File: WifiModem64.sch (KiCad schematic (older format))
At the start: 29 parts, among them J1 C64-UserPort, J2 USB_B, Q1 BSS138, Q2 BSS138, Q3 BSS138, Q4 BSS138, SW1 Push, SW2 Reset, U1 WeMos_mini, U2 WeMos_D1_mini_OLED_Shield

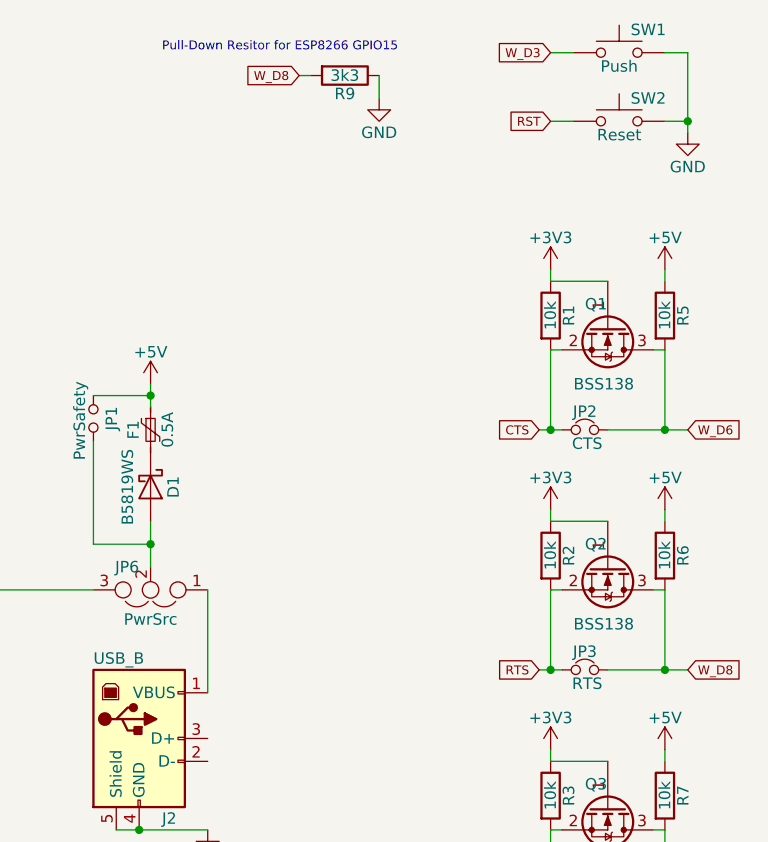
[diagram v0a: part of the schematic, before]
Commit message: Freed GPIO15 and fixed footprints.
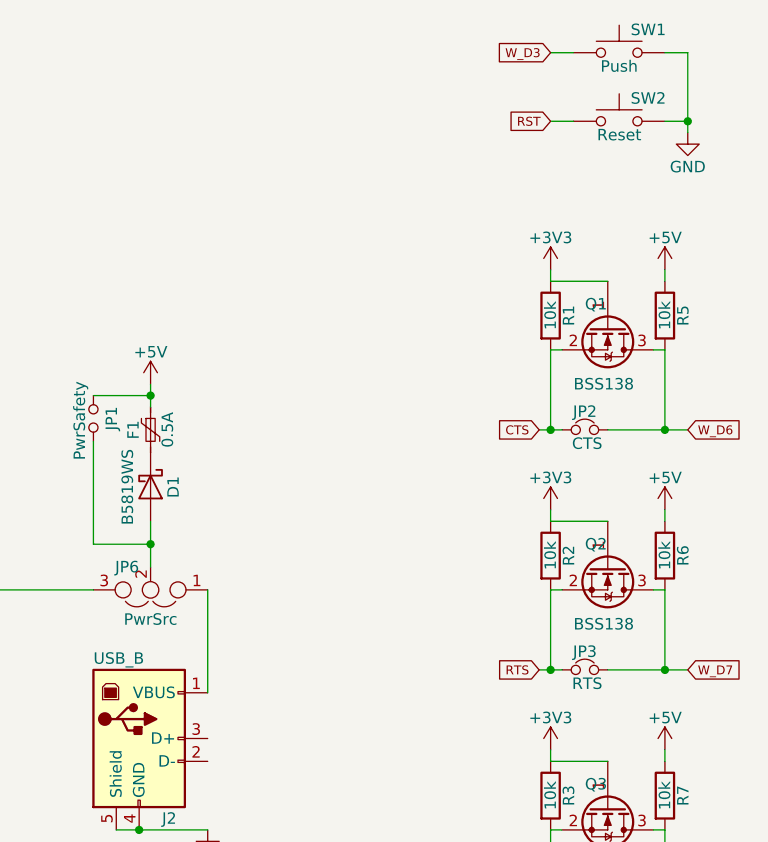
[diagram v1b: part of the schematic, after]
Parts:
- removed R9: 3k3, Resistors_THT:R_Axial_DIN0207_L6.3mm_D2.5mm_P7.62mm_Horizontal, symbol device:R
- D1: footprint Diodes_SMD:D_0805 -> Diodes_SMD:D_SOD-323_HandSoldering
- Q1, Q2, Q3, Q4: footprint TO_SOT_Packages_SMD:SOT-23 -> TO_SOT_Packages_SMD:SOT-23_Handsoldering
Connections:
- net W_D7: now also JP3.2, Q2.3 (D), R6.2
- net W_D8: no longer JP3.2, Q2.3 (D), R6.2
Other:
- note removed: "Pull-Down Resitor for ESP8266 GPIO15"
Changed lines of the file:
@@
 F 0 "Q4" V 9900 5450 50  0000 L CNN
 F 1 "BSS138" V 10250 5400 50  0000 L CNN
-F 2 "TO_SOT_Packages_SMD:SOT-23" H 10200 5475 50  0001 L CIN
+F 2 "TO_SOT_Packages_SMD:SOT-23_Handsoldering" H 10200 5475 50  0001 L CIN
 F 3 "" H 10000 5550 50  0001 L CNN
 	1    10000 5550
@@
 F 0 "Q3" V 9900 4400 50  0000 L CNN
 F 1 "BSS138" V 10250 4350 50  0000 L CNN
-F 2 "TO_SOT_Packages_SMD:SOT-23" H 10200 4425 50  0001 L CIN
+F 2 "TO_SOT_Packages_SMD:SOT-23_Handsoldering" H 10200 4425 50  0001 L CIN
 F 3 "" H 10000 4500 50  0001 L CNN
 	1    10000 4500
@@
 RTS
 Text GLabel 10350 3900 2    39   Input ~ 0
-W_D8
+W_D7
 $Comp
 L transistors:BSS138 Q2
@@
 F 0 "Q2" V 9900 3350 50  0000 L CNN
 F 1 "BSS138" V 10250 3300 50  0000 L CNN
-F 2 "TO_SOT_Packages_SMD:SOT-23" H 10200 3375 50  0001 L CIN
+F 2 "TO_SOT_Packages_SMD:SOT-23_Handsoldering" H 10200 3375 50  0001 L CIN
 F 3 "" H 10000 3450 50  0001 L CNN
 	1    10000 3450
@@
 F 0 "Q1" V 9900 2300 50  0000 L CNN
 F 1 "BSS138" V 10250 2250 50  0000 L CNN
-F 2 "TO_SOT_Packages_SMD:SOT-23" H 10200 2325 50  0001 L CIN
+F 2 "TO_SOT_Packages_SMD:SOT-23_Handsoldering" H 10200 2325 50  0001 L CIN
 F 3 "" H 10000 2400 50  0001 L CNN
 	1    10000 2400
@@
 F 0 "D1" H 8000 3200 50  0000 C CNN
 F 1 "B5819WS" H 8000 3000 50  0000 C CNN
-F 2 "Diodes_SMD:D_0805" H 8000 3100 50  0001 C CNN
+F 2 "Diodes_SMD:D_SOD-323_HandSoldering" H 8000 3100 50  0001 C CNN
 F 3 "" H 8000 3100 50  0001 C CNN
 	1    8000 3100
@@
 	7750 3350 8000 3350
 Connection ~ 8000 3350
-$Comp
-L power:GND #PWR022
-U 1 1 5A3817EF
-P 9000 1400
-F 0 "#PWR022" H 9000 1150 50  0001 C CNN
-F 1 "GND" H 9000 1250 50  0000 C CNN
-F 2 "" H 9000 1400 50  0001 C CNN
-F 3 "" H 9000 1400 50  0001 C CNN
-	1    9000 1400
-	1    0    0    -1
-$EndComp
-Text GLabel 8650 1300 0    39   Input ~ 0
-W_D8
-$Comp
-L device:R R9
-U 1 1 5A381890
-P 8850 1300
-F 0 "R9" V 8930 1300 50  0000 C CNN
-F 1 "3k3" V 8850 1300 50  0000 C CNN
-F 2 "Resistors_THT:R_Axial_DIN0207_L6.3mm_D2.5mm_P7.62mm_Horizontal" V 8780 1300 50  0001 C CNN
-F 3 "" H 8850 1300 50  0001 C CNN
-	1    8850 1300
-	0    1    1    0
-$EndComp
-Wire Wire Line
-	8650 1300 8700 1300
-Wire Wire Line
-	9000 1300 9000 1400
-Text Notes 8050 1200 0    39   ~ 0
-Pull-Down Resitor for ESP8266 GPIO15
 Wire Wire Line
 	5500 3550 5550 3550

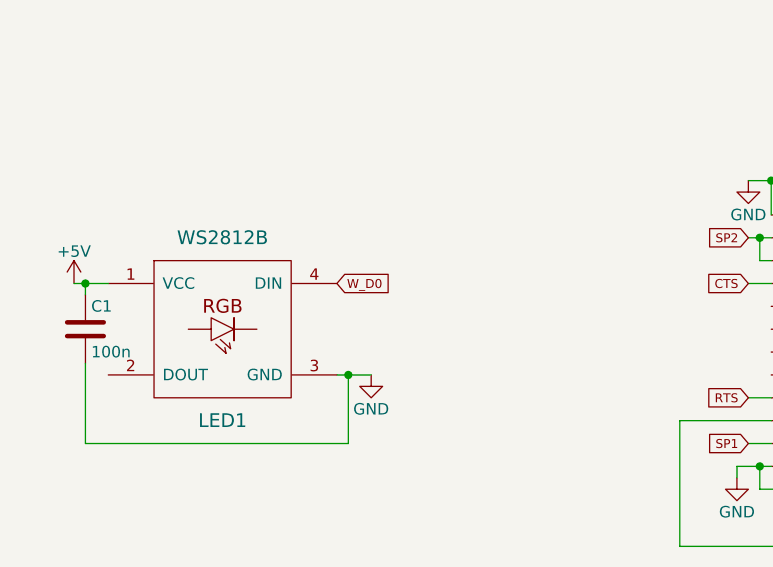
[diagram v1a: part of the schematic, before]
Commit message: WS2812b not working on D0.
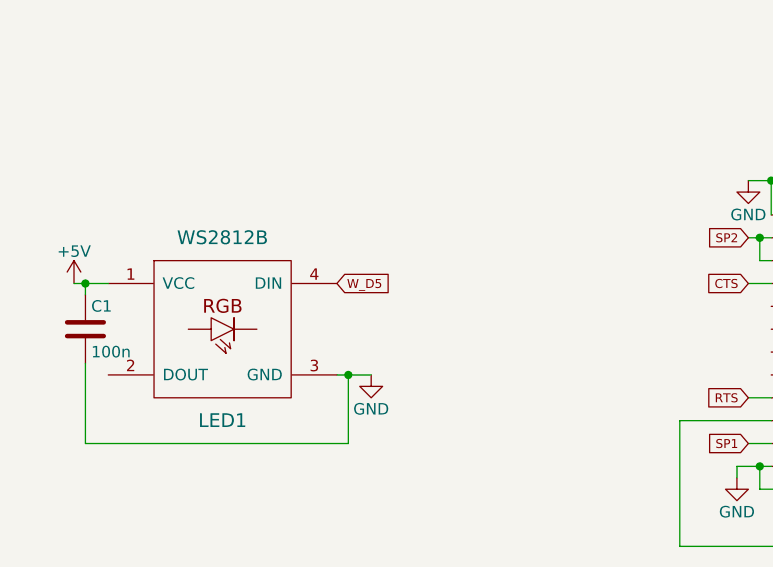
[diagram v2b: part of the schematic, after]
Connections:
- net W_D0: no longer LED1.4 (DIN)
- net W_D5: now also LED1.4 (DIN)
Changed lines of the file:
@@
 $EndComp
 Text GLabel 3650 3750 2    39   Input ~ 0
-W_D0
+W_D5
 $Comp
 L WifiModem64:WS2812B LED1
